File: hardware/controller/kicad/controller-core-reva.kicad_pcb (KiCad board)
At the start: 2 copper layers, 141.6 x 135.2 mm, 158 parts, among them J101 12V_ISOLATED_INPUT / JST XH, J102 STM_SWD / 1x6 2.54mm, J103 ESP_UART / 1x6 2.54mm, J104 UI_LINK / IDC 2x8 2.54mm, J105 JP13 NTC / 2 vías, J106 JP5 FLOW ADAPTER / VCC-GND-OC, J107 JP14 DOOR / contacto seco, J108 JP16 VISUAL V1..V8 / XH-8, J109 JP22 WATER / RED-WHITE-BLACK, J110 USB-C SERVICE / USB 2.0, J111 USB BENCH POWER / OPEN, J112 24V_ACTUATOR_INPUT / JST XH, J113 JP3 VALVE / JST XH, J114 POWER MONITOR / MEASURE ONLY, J115 JP8 GRINDER / 320VDC, J117 JP24 PUMP / 230VAC, J118 JP17 MAINS / L-N, J121 24V INTERNAL SELECT / OPEN FO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, K701 G5RL-1A-E-TV8 DC24, Q501 SI2308A, Q701 SI2308A / relay coil, U101 STM32G431RBT6, U201 ESP32-S3-WROOM-1-N8R8, U203 USBLC6-2SC6, U301 AP63203WU-7, U302 TPS22918DBVR, U303 AP63200WU-7 / 24V to 12V, U501 DRV8876PWPR, U502 UCC27517DBVR, U601 TPS3828-33DBVR, U602 SN74LVC2G08DCTR, U603 SN74LVC2G08DCTR

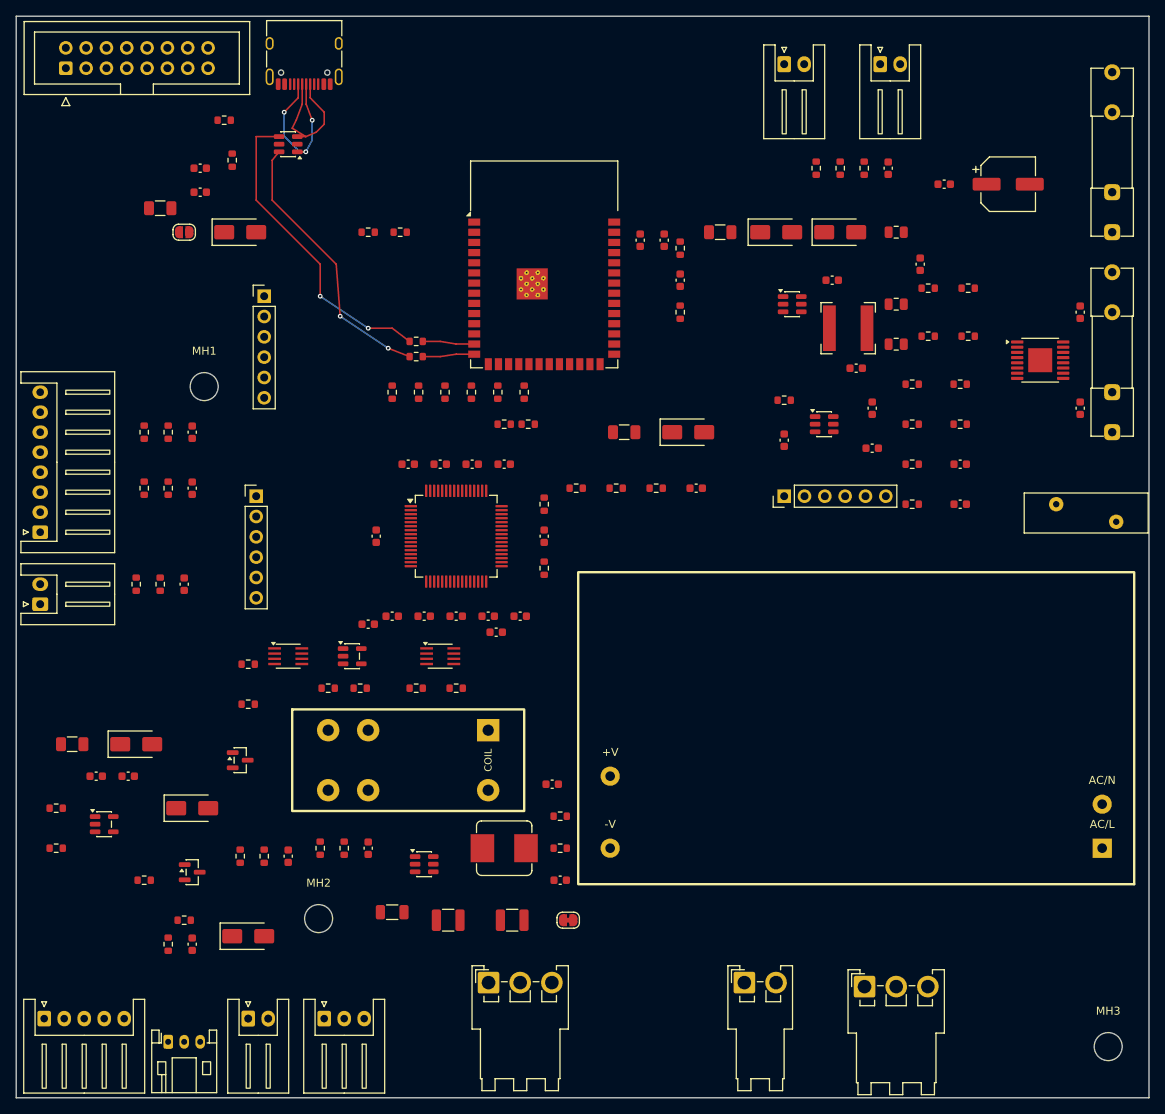
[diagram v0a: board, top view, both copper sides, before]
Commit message: Enforce mains/SELV barrier and route STM32 supply
Add a Mains net class and custom DRC rules: 8 mm clearance and creepage
between primary copper and SELV, 2.5 mm between distinct mains tracks.
The rule exposes 95 violations from the existing mains placement
(F701/F702 beside the H-bridge, K701 in the logic area, J115 beside the
12 V buck), so no mains copper is routed yet.

Route the STM32 supply: VDD ring under the LQFP, one VSS via per pin,
decoupling capacitors moved to their VDD/VSS pairs, and a provisional
B.Cu GND_UI plane that the filler keeps 8 mm from mains copper.

Co-Authored-By: Claude Opus 5 <noreply@anthropic.com>
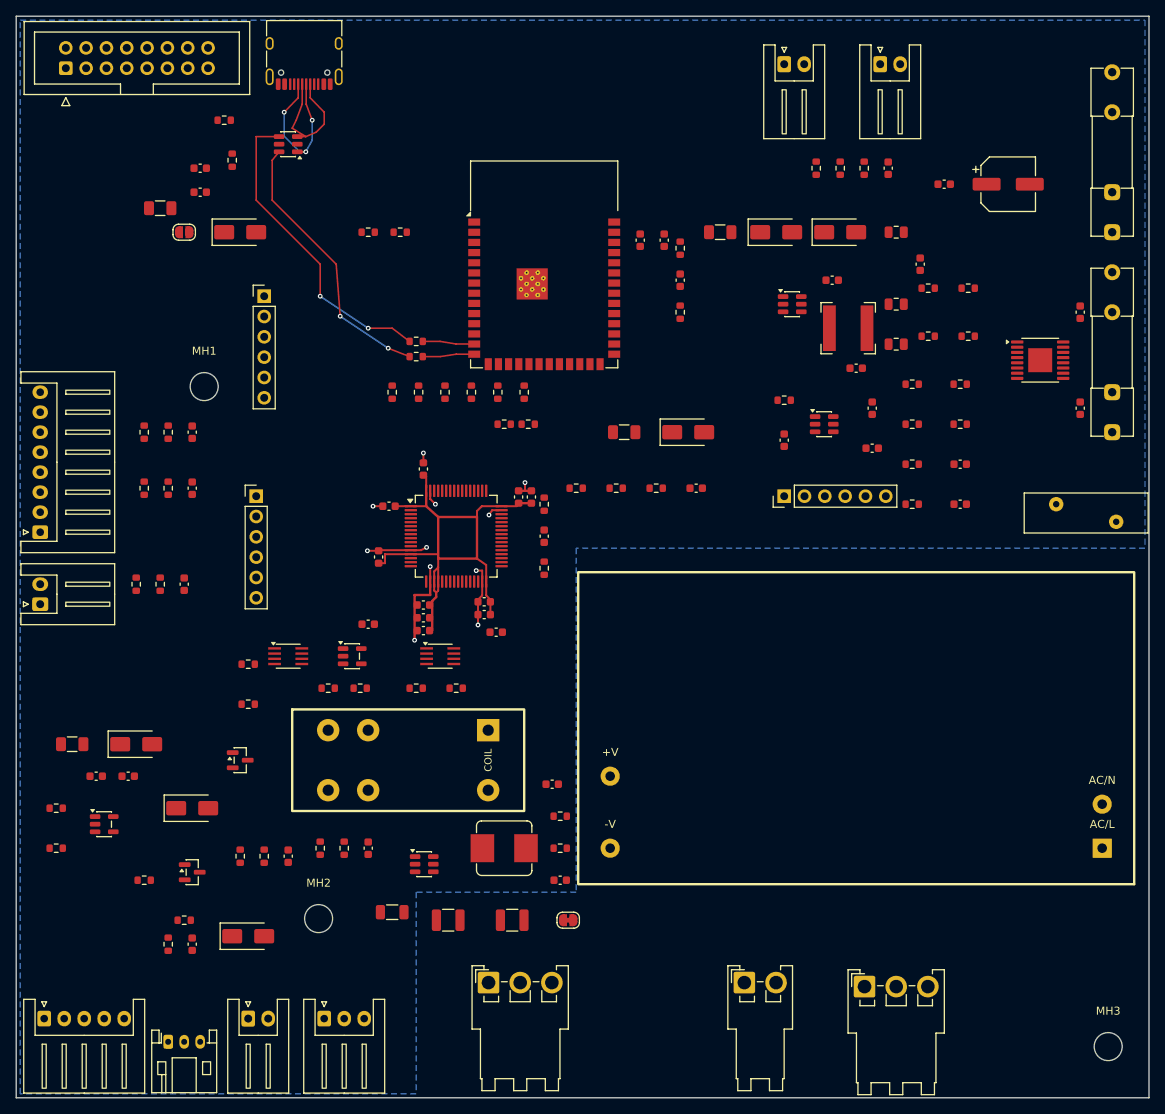
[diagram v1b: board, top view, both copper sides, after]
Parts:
- moved C106 22.9 mm to (64.4, 60.1), turned to 90 degrees
- moved C103 18.1 mm to (58.5, 73.2), turned to 180 degrees
- moved C102 12.2 mm to (45.3, 67.6), turned to 90 degrees
- moved C105 10.1 mm to (50.9, 56.6), turned to 90 degrees
- moved C109 8.10 mm to (50.9, 75.2), turned to 180 degrees
- moved C104 7.10 mm to (62.8, 60.1), turned to 90 degrees
- moved C110 4.50 mm to (58.5, 74.8), turned to 180 degrees
- moved C108 4.48 mm to (50.9, 76.8), turned to 180 degrees
- moved C111 4.08 mm to (46.6, 61.2), turned to 180 degrees
- moved C107 1.40 mm to (50.9, 73.6), turned to 180 degrees
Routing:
- net /3V3_CORE: track 0.00 -> 62.1 mm
- net /GND_UI: track 0.00 -> 32.7 mm, vias 0 -> 11
- added copper zone on B.Cu, net /GND_UI

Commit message: Move mains parts into a contiguous primary domain
Stand PS701 on the right edge with its AC pins beside J118 and its 24 V
pins in SELV. Group F701, F702 and RV701 between J118 and K701, which now
straddles the barrier with its coil in SELV. Move the 12 V buck beside
J112 and compact the DRV8876 block above PS701.

Draw the barrier centre line in layout_controller_pcb.py and keep an
8 mm copper/via/pad keepout band around it; the SELV ground plane now
stops at that band. DRC with all severities reports 0 violations.

Co-Authored-By: Claude Opus 5 <noreply@anthropic.com>
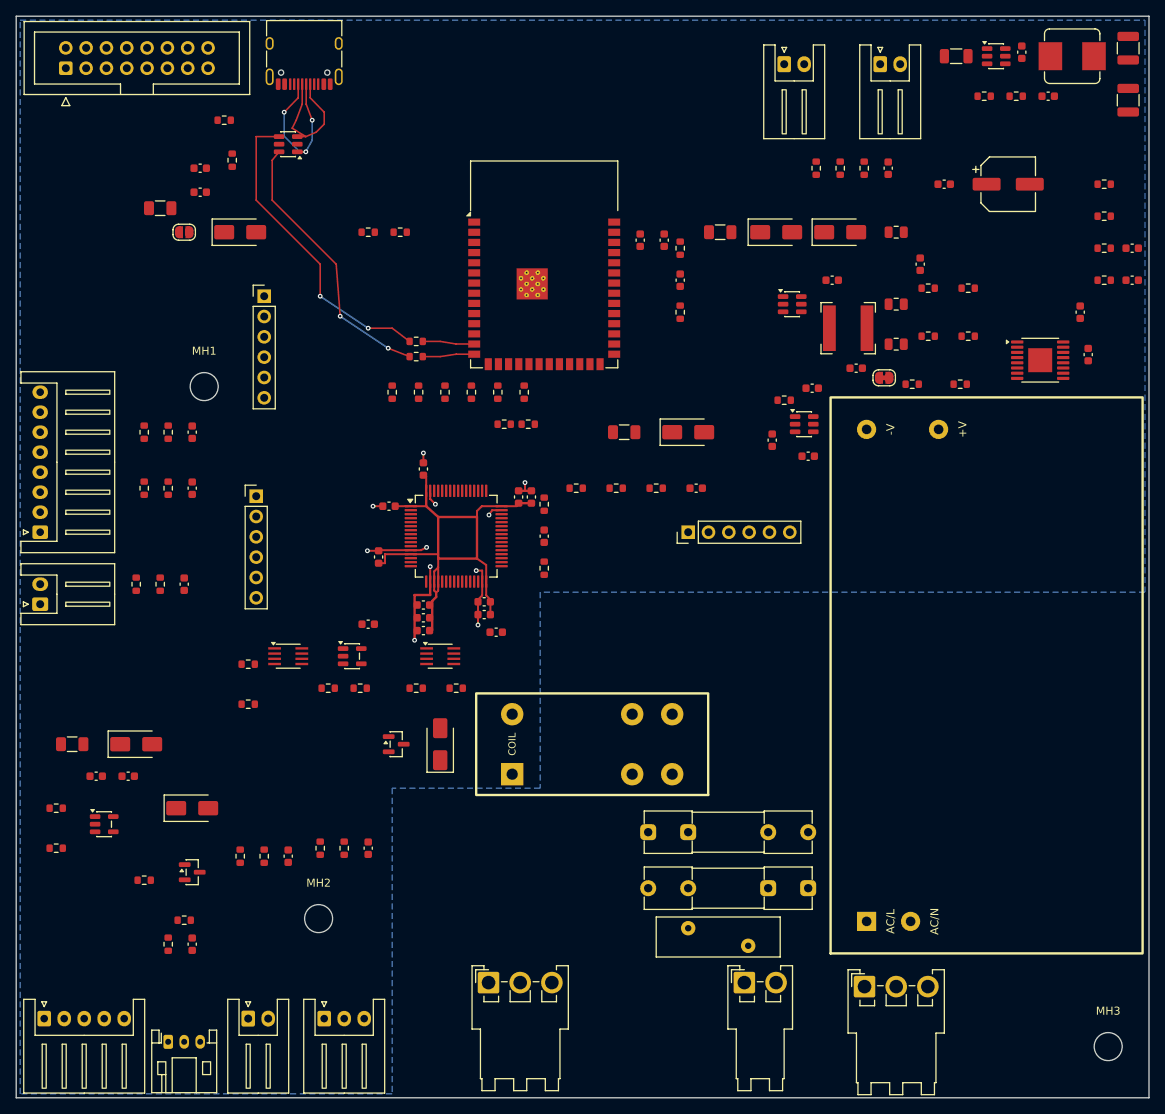
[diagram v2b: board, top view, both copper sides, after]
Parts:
- moved C311 138.2 mm to (139.0, 4.00), turned to 90 degrees
- moved C312 128.2 mm to (139.0, 10.5), turned to 90 degrees
- moved C310 128.1 mm to (117.5, 5.00)
- moved U303 123.7 mm to (122.5, 5.00)
- moved L302 121.8 mm to (132.0, 5.00)
- moved C314 115.4 mm to (129.0, 10.0)
- moved R303 109.9 mm to (125.0, 10.0)
- moved C313 108.7 mm to (125.7, 4.50), turned to -90 degrees
- moved R302 104.4 mm to (121.0, 10.0)
- moved F702 94.8 mm to (79.0, 102.0), turned to 0 degrees
- moved J121 78.5 mm to (108.5, 45.2)
- moved RV701 70.2 mm to (84.0, 114.0)
- moved F701 68.5 mm to (99.0, 109.0), turned to 180 degrees
- moved R507 38.4 mm to (136.0, 21.0)
- moved R510 36.9 mm to (136.0, 33.0)
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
